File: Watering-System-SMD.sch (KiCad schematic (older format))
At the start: 20 parts, among them CON1 AVR-ISP-6, J1 Screw_Terminal_1x02, J2 CONN_01X04_MALE, J3 Screw_Terminal_1x04, J4 Screw_Terminal_1x02, Q1 MMBF170, Q2 2N7002, U1 MCP1703A-3302/MB, U2 ATTINY85-20SU

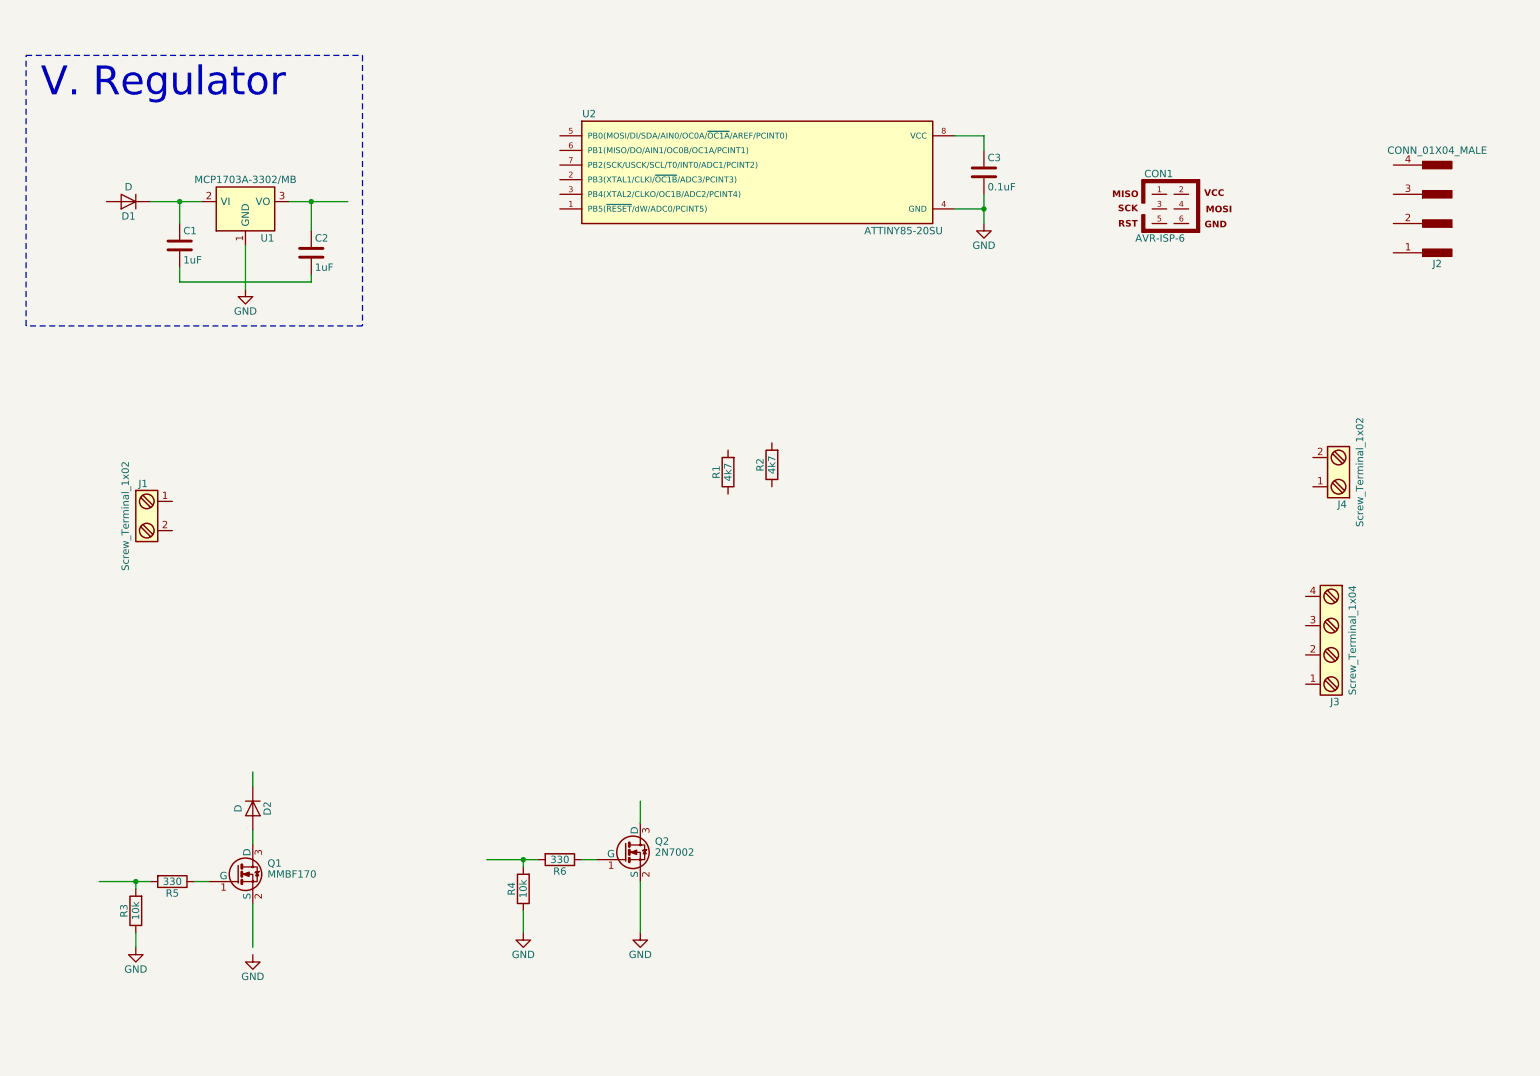
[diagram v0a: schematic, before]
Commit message: ESP-01 added
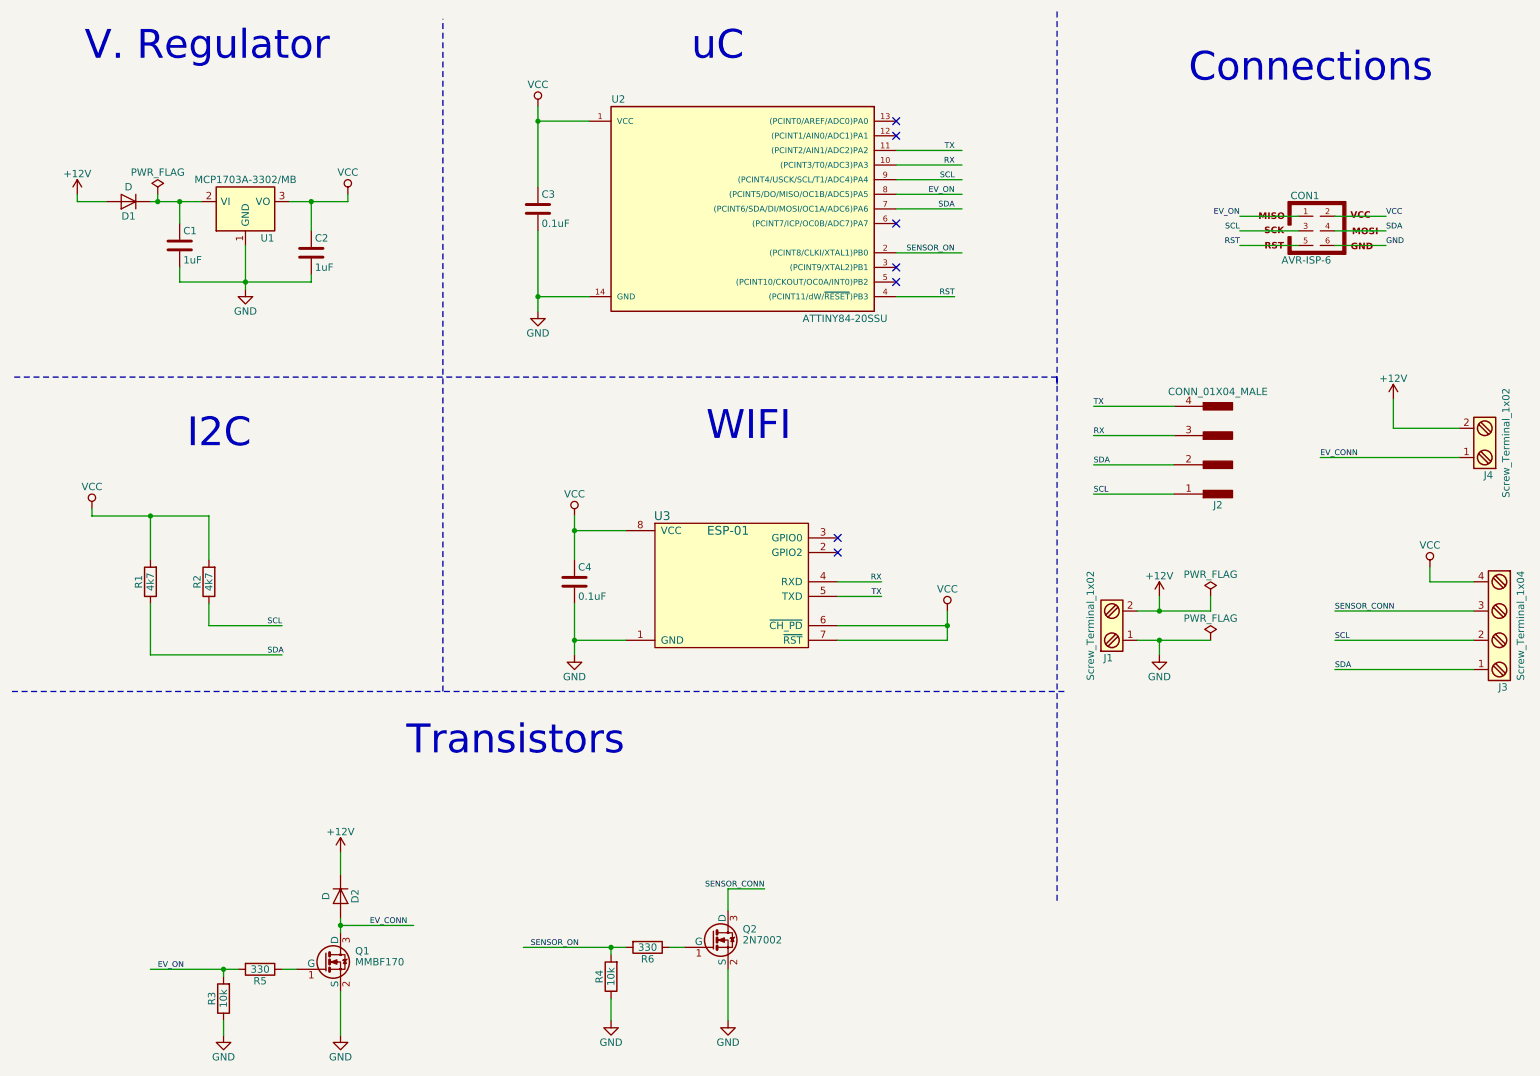
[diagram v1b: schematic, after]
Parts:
- removed U2: ATTINY85-20SU, Housings_SOIC:SOIC-8_3.9x4.9mm_Pitch1.27mm, symbol ATTINY85-20SU
- added C4: 0.1uF, Capacitors_SMD:C_0805_HandSoldering, symbol C
- added U2: ATTINY84-20SSU, SMD_Packages:SOIC-14_N, symbol ATTINY84-20SSU
- added U3: ESP-01, symbol ESP-01
- C1, C2, C3: footprint (none) -> Capacitors_SMD:C_0805_HandSoldering
- CON1: footprint AVR-ISP-6 -> Pin_Headers:Pin_Header_Straight_2x03_Pitch2.54mm
- D1, D2: footprint (none) -> Diodes_SMD:D_SMA_Handsoldering
- J1: footprint (none) -> Terminal_Blocks:TerminalBlock_Pheonix_MKDS1.5-2pol
- J2: footprint (none) -> Pin_Headers:Pin_Header_Straight_1x04_Pitch2.54mm
- J3: footprint (none) -> Terminal_Blocks:TerminalBlock_Pheonix_MPT-2.54mm_4pol
- J4: footprint (none) -> Terminal_Blocks:TerminalBlock_Pheonix_MPT-2.54mm_2pol
- R1, R2, R3, R4, R5, R6: footprint (none) -> Resistors_SMD:R_0805_HandSoldering
- U1: footprint TO_SOT_Packages_SMD:SOT89-3_Housing -> TO_SOT_Packages_SMD:SOT-89-3_Handsoldering
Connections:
- net labels added: +12V, EV_CONN, EV_ON, RST, RX, SCL, SDA, SENSOR_CONN, SENSOR_ON, TX, VCC
- wire segments 25 -> 78
- no-connect marks 0 -> 7
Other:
- note added: "Connections"
- note added: "I2C"
- note added: "Transistors"
- note added: "WIFI"
- note added: "uC"
- moved on the sheet: C3, CON1, D2, J1, J2, J3, J4, Q1, Q2, R1, R2, R3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

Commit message: PCB routed
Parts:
- removed C4: 0.1uF, Capacitors_SMD:C_0805_HandSoldering, symbol C
- U3: footprint (none) -> ESP8266:ESP-01
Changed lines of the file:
@@
 $EndComp
 $Comp
-L GND #PWR4
+L GND #PWR01
 U 1 1 59232D52
 P 2100 2350
-F 0 "#PWR4" H 2100 2100 50  0001 C CNN
+F 0 "#PWR01" H 2100 2100 50  0001 C CNN
 F 1 "GND" H 2100 2200 50  0000 C CNN
 F 2 "" H 2100 2350 50  0001 C CNN
@@
 V. Regulator
 $Comp
-L GND #PWR12
+L GND #PWR02
 U 1 1 592397F1
 P 4100 2500
-F 0 "#PWR12" H 4100 2250 50  0001 C CNN
+F 0 "#PWR02" H 4100 2250 50  0001 C CNN
 F 1 "GND" H 4100 2350 50  0000 C CNN
 F 2 "" H 4100 2500 50  0001 C CNN
@@
 $EndComp
 $Comp
-L GND #PWR3
+L GND #PWR03
 U 1 1 59239E0F
 P 1950 7450
-F 0 "#PWR3" H 1950 7200 50  0001 C CNN
+F 0 "#PWR03" H 1950 7200 50  0001 C CNN
 F 1 "GND" H 1950 7300 50  0000 C CNN
 F 2 "" H 1950 7450 50  0001 C CNN
@@
 $EndComp
 $Comp
-L GND #PWR6
+L GND #PWR04
 U 1 1 59239E4B
 P 2750 7450
-F 0 "#PWR6" H 2750 7200 50  0001 C CNN
+F 0 "#PWR04" H 2750 7200 50  0001 C CNN
 F 1 "GND" H 2750 7300 50  0000 C CNN
 F 2 "" H 2750 7450 50  0001 C CNN
@@
 $EndComp
 $Comp
-L GND #PWR8
+L GND #PWR05
 U 1 1 5923AC87
 P 4600 7350
-F 0 "#PWR8" H 4600 7100 50  0001 C CNN
+F 0 "#PWR05" H 4600 7100 50  0001 C CNN
 F 1 "GND" H 4600 7200 50  0000 C CNN
 F 2 "" H 4600 7350 50  0001 C CNN
@@
 $EndComp
 $Comp
-L GND #PWR13
+L GND #PWR06
 U 1 1 5923ACD5
 P 5400 7350
-F 0 "#PWR13" H 5400 7100 50  0001 C CNN
+F 0 "#PWR06" H 5400 7100 50  0001 C CNN
 F 1 "GND" H 5400 7200 50  0000 C CNN
 F 2 "" H 5400 7350 50  0001 C CNN
@@
 $EndComp
 $Comp
-L VCC #PWR7
+L VCC #PWR07
 U 1 1 5924673B
 P 2800 1700
-F 0 "#PWR7" H 2800 1550 50  0001 C CNN
+F 0 "#PWR07" H 2800 1550 50  0001 C CNN
 F 1 "VCC" H 2800 1850 50  0000 C CNN
 F 2 "" H 2800 1700 50  0001 C CNN
@@
 $EndComp
 $Comp
-L VCC #PWR11
+L VCC #PWR08
 U 1 1 59246DC4
 P 4100 1100
-F 0 "#PWR11" H 4100 950 50  0001 C CNN
+F 0 "#PWR08" H 4100 950 50  0001 C CNN
 F 1 "VCC" H 4100 1250 50  0000 C CNN
 F 2 "" H 4100 1100 50  0001 C CNN
@@
 $EndComp
 $Comp
-L +12V #PWR5
+L +12V #PWR09
 U 1 1 59246F52
 P 2750 6200
-F 0 "#PWR5" H 2750 6050 50  0001 C CNN
+F 0 "#PWR09" H 2750 6050 50  0001 C CNN
 F 1 "+12V" H 2750 6340 50  0000 C CNN
 F 2 "" H 2750 6200 50  0001 C CNN
@@
 SENSOR_CONN
 $Comp
-L +12V #PWR17
+L +12V #PWR010
 U 1 1 59248FF3
 P 9950 3100
-F 0 "#PWR17" H 9950 2950 50  0001 C CNN
+F 0 "#PWR010" H 9950 2950 50  0001 C CNN
 F 1 "+12V" H 9950 3240 50  0000 C CNN
 F 2 "" H 9950 3100 50  0001 C CNN
@@
 EV_CONN
 $Comp
-L +12V #PWR15
+L +12V #PWR011
 U 1 1 59249304
 P 8350 4450
-F 0 "#PWR15" H 8350 4300 50  0001 C CNN
+F 0 "#PWR011" H 8350 4300 50  0001 C CNN
 F 1 "+12V" H 8350 4590 50  0000 C CNN
 F 2 "" H 8350 4450 50  0001 C CNN
@@
 $EndComp
 $Comp
-L GND #PWR16
+L GND #PWR012
 U 1 1 59249340
 P 8350 4850
-F 0 "#PWR16" H 8350 4600 50  0001 C CNN
+F 0 "#PWR012" H 8350 4600 50  0001 C CNN
 F 1 "GND" H 8350 4700 50  0000 C CNN
 F 2 "" H 8350 4850 50  0001 C CNN
@@
 $EndComp
 $Comp
-L VCC #PWR18
+L VCC #PWR013
 U 1 1 5924995F
 P 10200 4250
-F 0 "#PWR18" H 10200 4100 50  0001 C CNN
+F 0 "#PWR013" H 10200 4100 50  0001 C CNN
 F 1 "VCC" H 10200 4400 50  0000 C CNN
 F 2 "" H 10200 4250 50  0001 C CNN
@@
 SDA
 $Comp
-L VCC #PWR2
+L VCC #PWR014
 U 1 1 5924A418
 P 1050 3850
-F 0 "#PWR2" H 1050 3700 50  0001 C CNN
+F 0 "#PWR014" H 1050 3700 50  0001 C CNN
 F 1 "VCC" H 1050 4000 50  0000 C CNN
 F 2 "" H 1050 3850 50  0001 C CNN
@@
 SENSOR_CONN
 $Comp
-L +12V #PWR1
+L +12V #PWR015
 U 1 1 5924CCAD
 P 950 1700
-F 0 "#PWR1" H 950 1550 50  0001 C CNN
+F 0 "#PWR015" H 950 1550 50  0001 C CNN
 F 1 "+12V" H 950 1840 50  0000 C CNN
 F 2 "" H 950 1700 50  0001 C CNN
@@
 GND
 $Comp
-L PWR_FLAG #FLG2
+L PWR_FLAG #FLG016
 U 1 1 5924EA09
 P 8700 4450
-F 0 "#FLG2" H 8700 4525 50  0001 C CNN
+F 0 "#FLG016" H 8700 4525 50  0001 C CNN
 F 1 "PWR_FLAG" H 8700 4600 50  0000 C CNN
 F 2 "" H 8700 4450 50  0001 C CNN
@@
 $EndComp
 $Comp
-L PWR_FLAG #FLG3
+L PWR_FLAG #FLG017
 U 1 1 5924EA57
 P 8700 4750
-F 0 "#FLG3" H 8700 4825 50  0001 C CNN
+F 0 "#FLG017" H 8700 4825 50  0001 C CNN
 F 1 "PWR_FLAG" H 8700 4900 50  0000 C CNN
 F 2 "" H 8700 4750 50  0001 C CNN
@@
 $EndComp
 $Comp
-L PWR_FLAG #FLG1
+L PWR_FLAG #FLG018
 U 1 1 5924F148
 P 1500 1700
-F 0 "#FLG1" H 1500 1775 50  0001 C CNN
+F 0 "#FLG018" H 1500 1775 50  0001 C CNN
 F 1 "PWR_FLAG" H 1500 1850 50  0000 C CNN
 F 2 "" H 1500 1700 50  0001 C CNN
@@
 Wire Wire Line
 	6550 1500 7000 1500
-Text Label 6950 1400 2    39   ~ 0
+Text Label 7000 1500 2    39   ~ 0
 TX
-Text Label 6950 1500 2    39   ~ 0
+Text Label 7000 1400 2    39   ~ 0
 RX
 NoConn ~ 6550 1900
@@
 F 0 "U3" H 4950 4000 60  0000 C CNN
 F 1 "ESP-01" H 5400 3900 60  0000 C CNN
-F 2 "" H 5600 4100 60  0001 C CNN
+F 2 "ESP8266:ESP-01" H 5600 4100 60  0001 C CNN
 F 3 "" H 5600 4100 60  0001 C CNN
 	1    4900 3950
@@
 $EndComp
 $Comp
-L C C4
-U 1 1 5942E50A
-P 4350 4350
-F 0 "C4" H 4375 4450 50  0000 L CNN
-F 1 "0.1uF" H 4375 4250 50  0000 L CNN
-F 2 "Capacitors_SMD:C_0805_HandSoldering" H 4388 4200 50  0001 C CNN
-F 3 "" H 4350 4350 50  0001 C CNN
-	1    4350 4350
-	1    0    0    -1
-$EndComp
-Wire Wire Line
-	4700 4000 4350 4000
-Wire Wire Line
-	4350 3900 4350 4200
-Wire Wire Line
-	4350 4500 4350 4850
-Wire Wire Line
-	4350 4750 4700 4750
-$Comp
-L VCC #PWR9
+L VCC #PWR019
 U 1 1 5942E6D8
-P 4350 3900
-F 0 "#PWR9" H 4350 3750 50  0001 C CNN
-F 1 "VCC" H 4350 4050 50  0000 C CNN
-F 2 "" H 4350 3900 50  0001 C CNN
-F 3 "" H 4350 3900 50  0001 C CNN
-	1    4350 3900
-	1    0    0    -1
-$EndComp
-$Comp
-L GND #PWR10
+P 4600 3900
+F 0 "#PWR019" H 4600 3750 50  0001 C CNN
+F 1 "VCC" H 4600 4050 50  0000 C CNN
+F 2 "" H 4600 3900 50  0001 C CNN
+F 3 "" H 4600 3900 50  0001 C CNN
+	1    4600 3900
+	1    0    0    -1
+$EndComp
+$Comp
+L GND #PWR020
 U 1 1 5942E954
-P 4350 4850
-F 0 "#PWR10" H 4350 4600 50  0001 C CNN
-F 1 "GND" H 4350 4700 50  0000 C CNN
-F 2 "" H 4350 4850 50  0001 C CNN
-F 3 "" H 4350 4850 50  0001 C CNN
-	1    4350 4850
-	1    0    0    -1
-$EndComp
-Connection ~ 4350 4000
-Connection ~ 4350 4750
+P 4600 4850
+F 0 "#PWR020" H 4600 4600 50  0001 C CNN
+F 1 "GND" H 4600 4700 50  0000 C CNN
+F 2 "" H 4600 4850 50  0001 C CNN
+F 3 "" H 4600 4850 50  0001 C CNN
+	1    4600 4850
+	1    0    0    -1
+$EndComp
 Wire Notes Line
 	7650 450  7650 6550
@@
 Connection ~ 6900 4650
 $Comp
-L VCC #PWR14
+L VCC #PWR021
 U 1 1 59432303
 P 6900 4550
-F 0 "#PWR14" H 6900 4400 50  0001 C CNN
+F 0 "#PWR021" H 6900 4400 50  0001 C CNN
 F 1 "VCC" H 6900 4700 50  0000 C CNN
 F 2 "" H 6900 4550 50  0001 C CNN
@@
 Text Notes 3200 5550 0    197  ~ 0
 Transistors
+Wire Wire Line
+	4700 4000 4600 4000
+Wire Wire Line
+	4600 4000 4600 3900
+Wire Wire Line
+	4700 4750 4600 4750
+Wire Wire Line
+	4600 4750 4600 4850
 $EndSCHEMATC

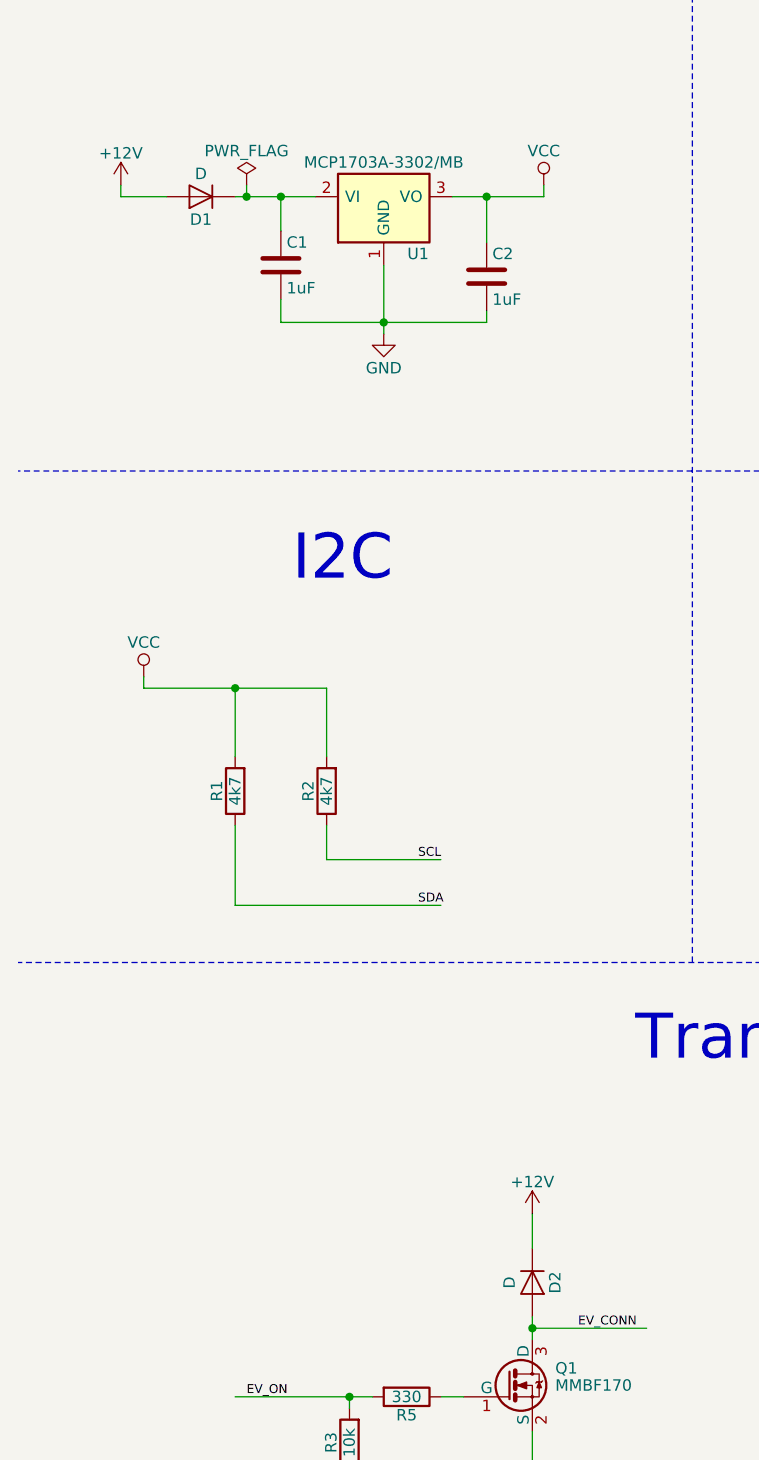
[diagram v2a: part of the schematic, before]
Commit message: SilkScreen changed
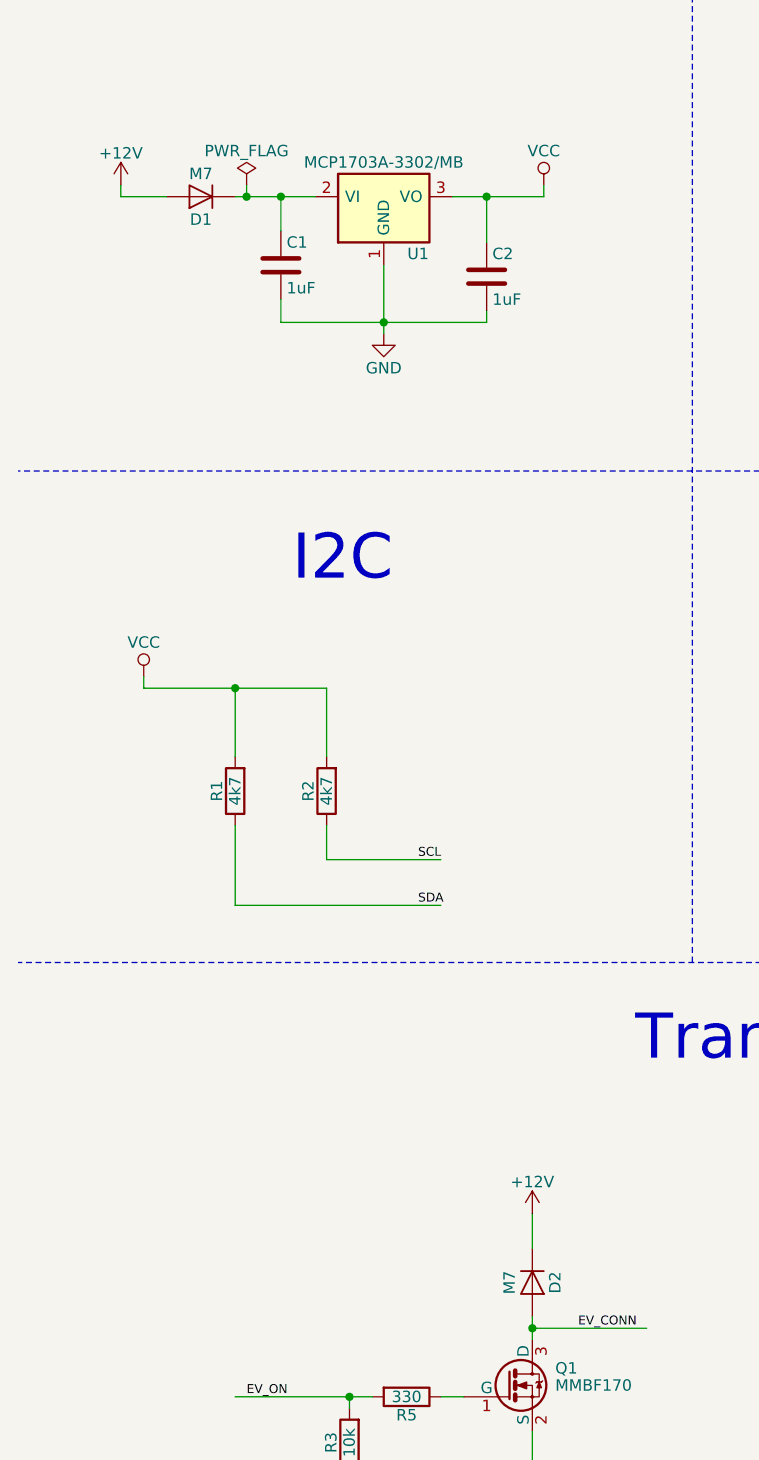
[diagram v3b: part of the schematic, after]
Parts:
- D1, D2: value D -> M7
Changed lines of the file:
@@
 P 1300 1750
 F 0 "D1" H 1300 1850 50  0000 C CNN
-F 1 "D" H 1300 1650 50  0000 C CNN
+F 1 "M7" H 1300 1650 50  0000 C CNN
 F 2 "Diodes_SMD:D_SMA_Handsoldering" H 1300 1750 50  0001 C CNN
 F 3 "" H 1300 1750 50  0001 C CNN
@@
 P 2750 6500
 F 0 "D2" H 2750 6600 50  0000 C CNN
-F 1 "D" H 2750 6400 50  0000 C CNN
+F 1 "M7" H 2750 6400 50  0000 C CNN
 F 2 "Diodes_SMD:D_SMA_Handsoldering" H 2750 6500 50  0001 C CNN
 F 3 "" H 2750 6500 50  0001 C CNN
